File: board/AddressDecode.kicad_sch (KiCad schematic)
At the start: 17 parts, among them U10 74LS154, U11 74F00, U12 74F02, U13 74F08, U14 74F32, U15 74F30, U16 74LS260, U17 74LS154, U18 74F04

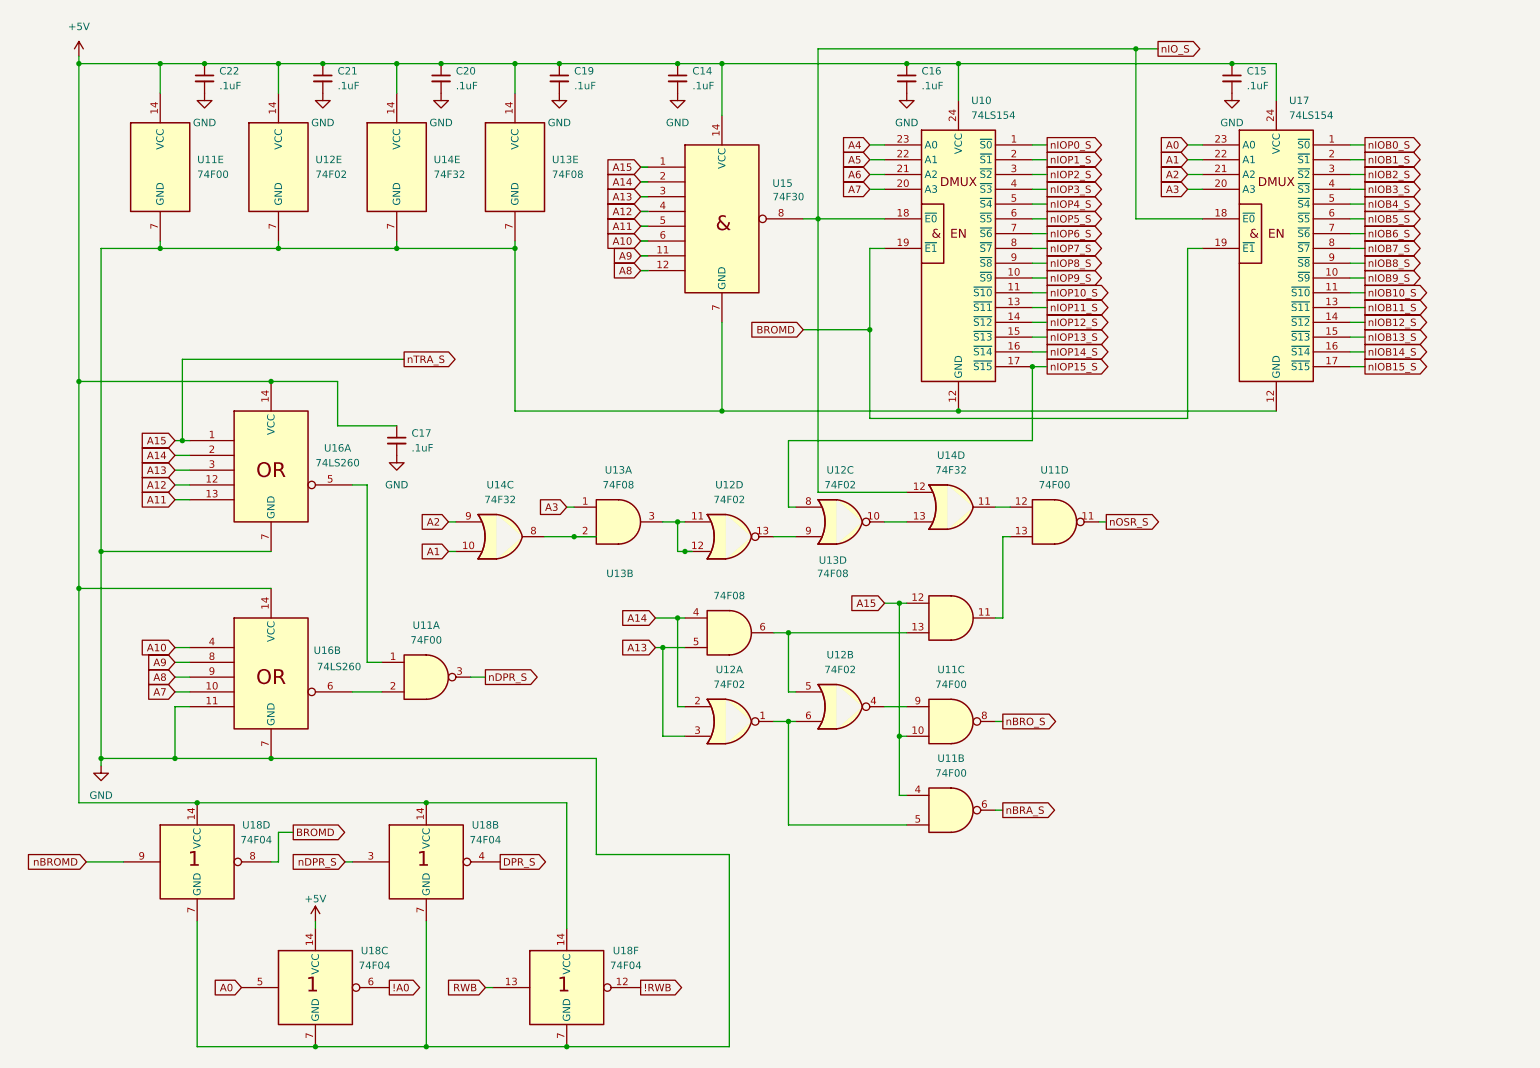
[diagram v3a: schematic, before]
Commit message: More main PCB updates.  Rearranged some things.  Bypass caps near PS connector.  Moved front panel connector to opposite side of board.
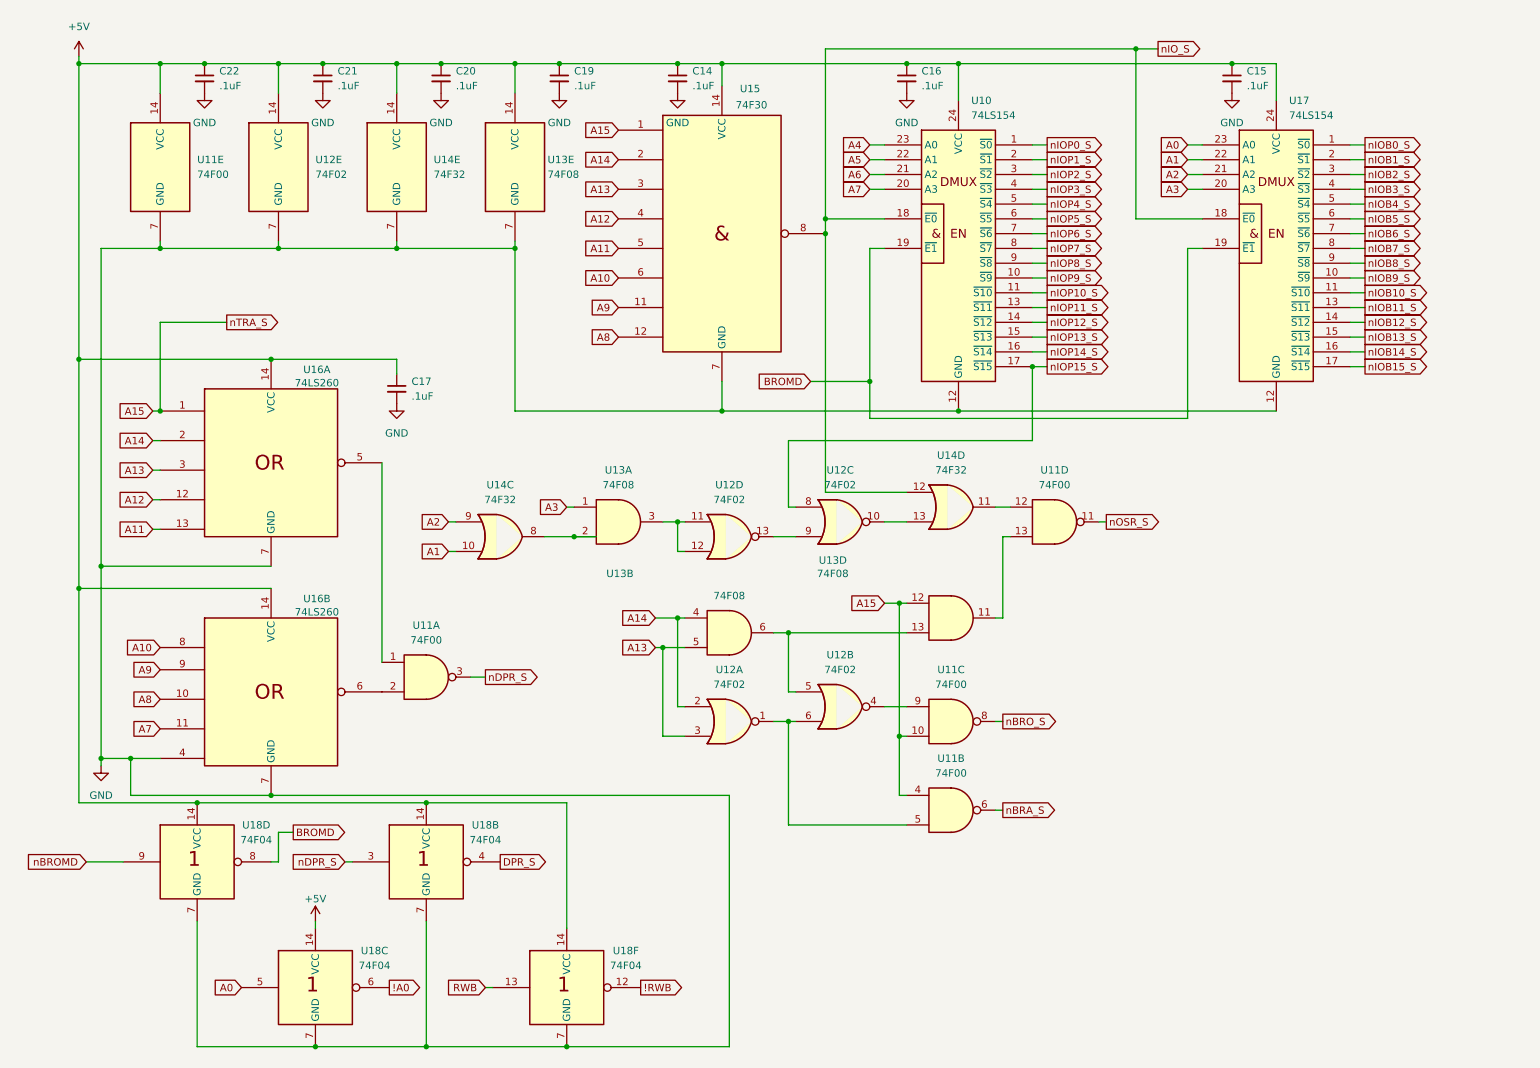
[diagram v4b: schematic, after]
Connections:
- net A10: now also U16.8; no longer U16.4
- net A7: now also U16.11; no longer U16.10
- net A8: now also U16.10; no longer U16.9
- net A9: now also U16.9; no longer U16.8
- net GND: now also U16.4; no longer U16.11
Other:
- moved on the sheet: C17, U15, U16A, U16B

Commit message: Latest main PCB update with FFF1 and FFF2 added and decode logic updated to exclude FFFE and FFFF in nOSROM_S signal
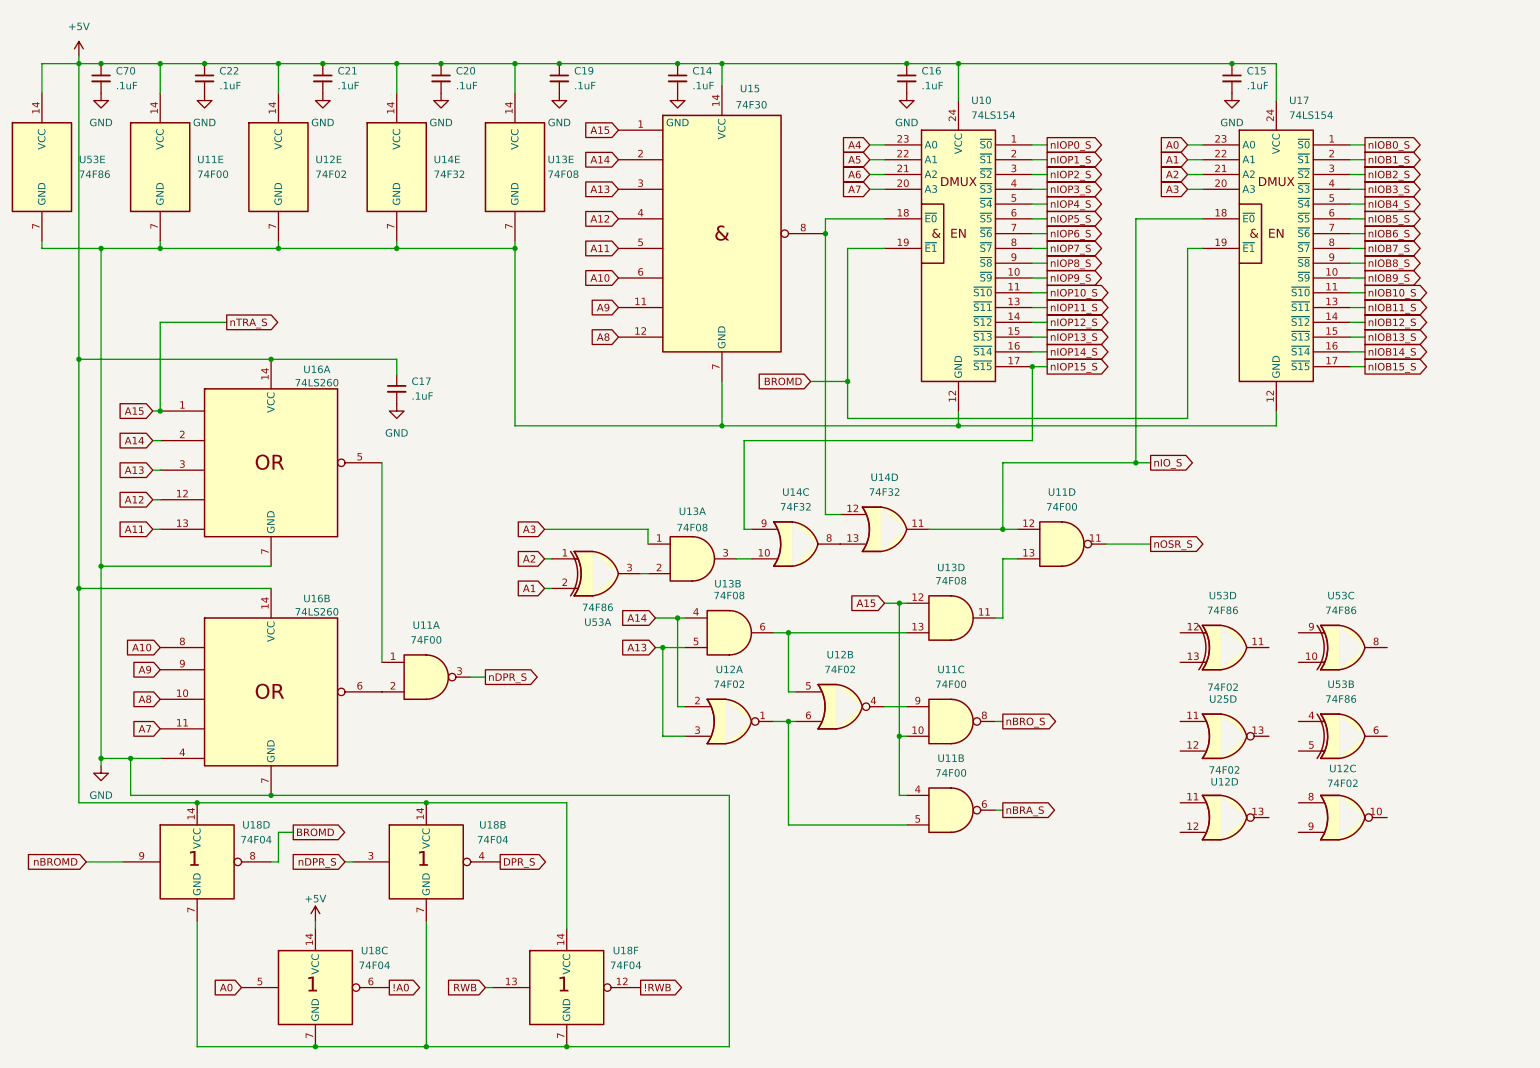
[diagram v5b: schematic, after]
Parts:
- added C70: .1uF, Capacitor_THT:C_Disc_D5.0mm_W2.5mm_P5.00mm, symbol Device:C_Small
- added U25: 74F02, Package_DIP:DIP-14_W7.62mm_Socket_LongPads, symbol 74xx:7402
- added U53: 74F86, Package_DIP:DIP-14_W7.62mm_Socket_LongPads, symbol 74xx:74LS86
- U10, U17: footprint Package_DIP:DIP-24_W15.24mm_LongPads -> Package_DIP:DIP-24_W15.24mm_Socket_LongPads
- U11, U13, U14, U15, U16, U18: footprint Package_DIP:DIP-14_W7.62mm_LongPads -> Package_DIP:DIP-14_W7.62mm_Socket_LongPads
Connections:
- net +5V: now also C70.1, U53.14 (VCC)
- net A1: now also U53.2; no longer U14.10
- net A2: now also U53.1; no longer U14.9
- net GND: now also C70.2, U53.7 (GND)
- net nIOP15_S: now also U14.9; no longer U12.8
- net nIO_S: now also U11.12, U14.11; no longer U10.18 (~{E0}), U14.12, U15.8
- net at U12.13: no longer U12.9
- net at U14.13: now also U14.8; no longer U12.10
- net at U13.2: now also U53.3; no longer U14.8
- new net: U13.3, U14.10
- new net: U10.18 (~{E0}), U14.12, U15.8
- now unconnected: U12.11, U12.12
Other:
- moved on the sheet: U11D, U14D

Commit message: Updated schematics with larger mounting holes (4mm vs 3.2mm) and larger electrolytic cap footprints
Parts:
- U12: footprint Package_DIP:DIP-14_W7.62mm_LongPads -> Package_DIP:DIP-14_W7.62mm_Socket_LongPads
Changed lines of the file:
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@@
 			)
 		)
-		(property "Footprint" "Package_DIP:DIP-14_W7.62mm_LongPads"
+		(property "Footprint" "Package_DIP:DIP-14_W7.62mm_Socket_LongPads"
 			(at 162.56 135.89 0)
 			(effects
@@
 			)
 		)
-		(property "Footprint" "Package_DIP:DIP-14_W7.62mm_LongPads"
+		(property "Footprint" "Package_DIP:DIP-14_W7.62mm_Socket_LongPads"
 			(at 143.51 138.43 0)
 			(effects
@@
 			)
 		)
-		(property "Footprint" "Package_DIP:DIP-14_W7.62mm_LongPads"
+		(property "Footprint" "Package_DIP:DIP-14_W7.62mm_Socket_LongPads"
 			(at 66.04 43.18 0)
 			(effects
@@
 			)
 		)
-		(property "Footprint" "Package_DIP:DIP-14_W7.62mm_LongPads"
+		(property "Footprint" "Package_DIP:DIP-14_W7.62mm_Socket_LongPads"
 			(at 228.6 154.94 0)
 			(effects
@@
 			)
 		)
-		(property "Footprint" "Package_DIP:DIP-14_W7.62mm_LongPads"
+		(property "Footprint" "Package_DIP:DIP-14_W7.62mm_Socket_LongPads"
 			(at 248.92 154.94 0)
 			(effects

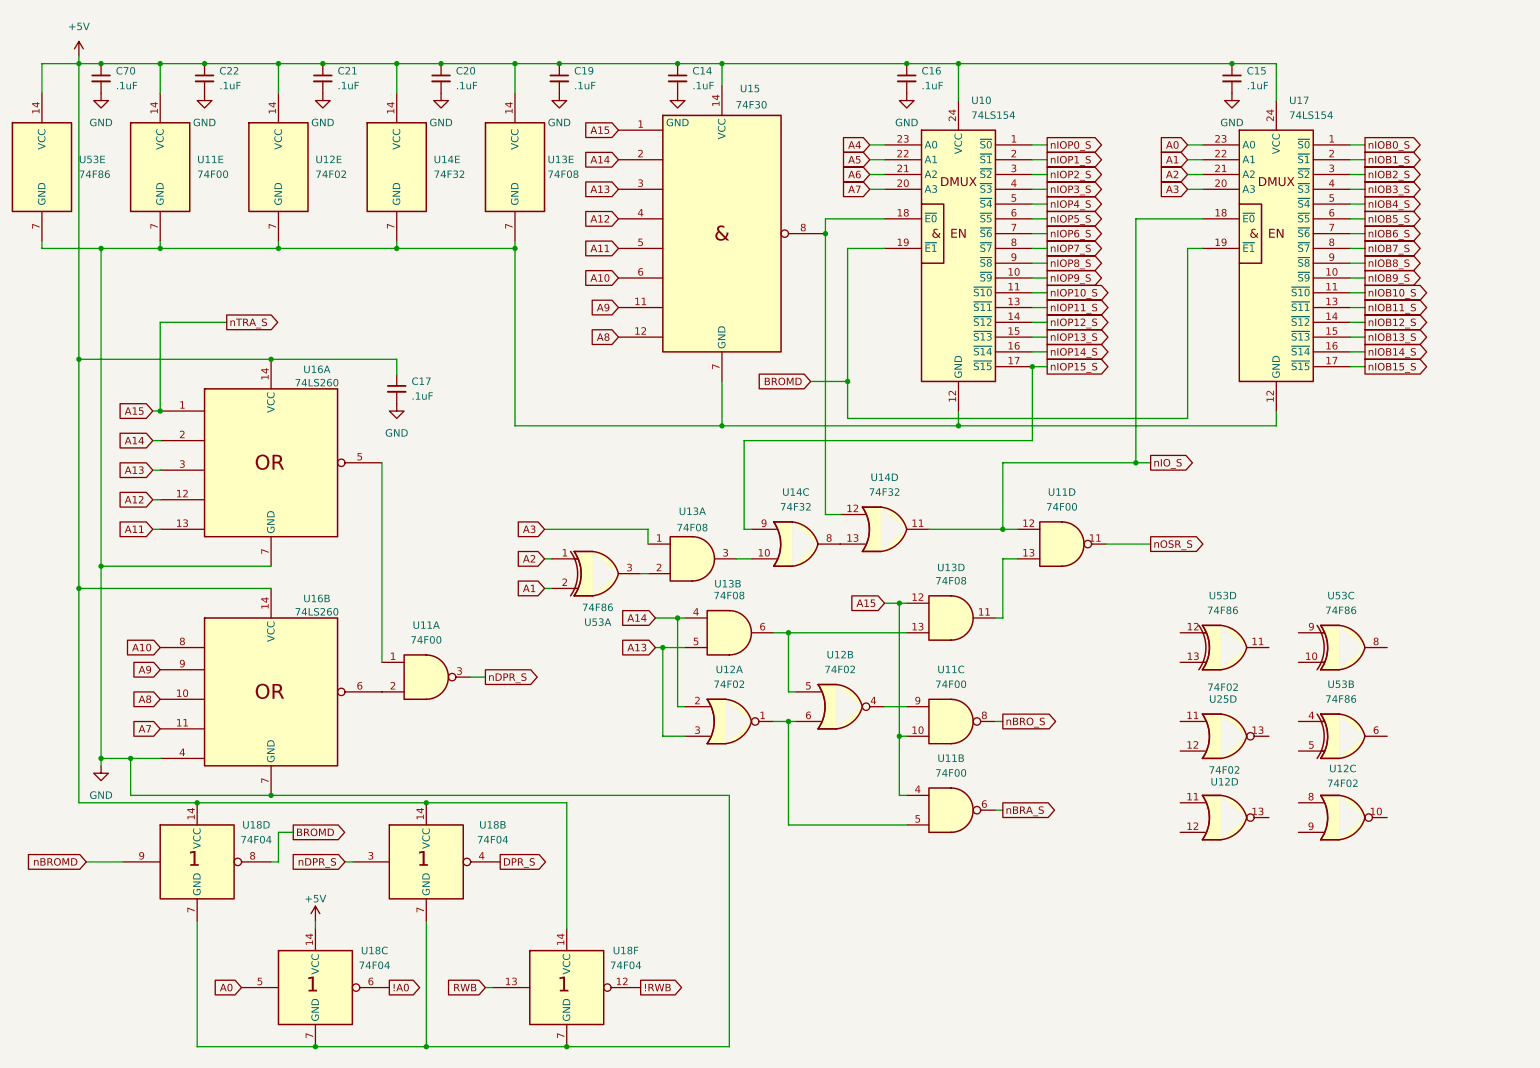
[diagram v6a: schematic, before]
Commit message: Schematic Bus updates, silkscreen updates, position tweaks, and other corrections.
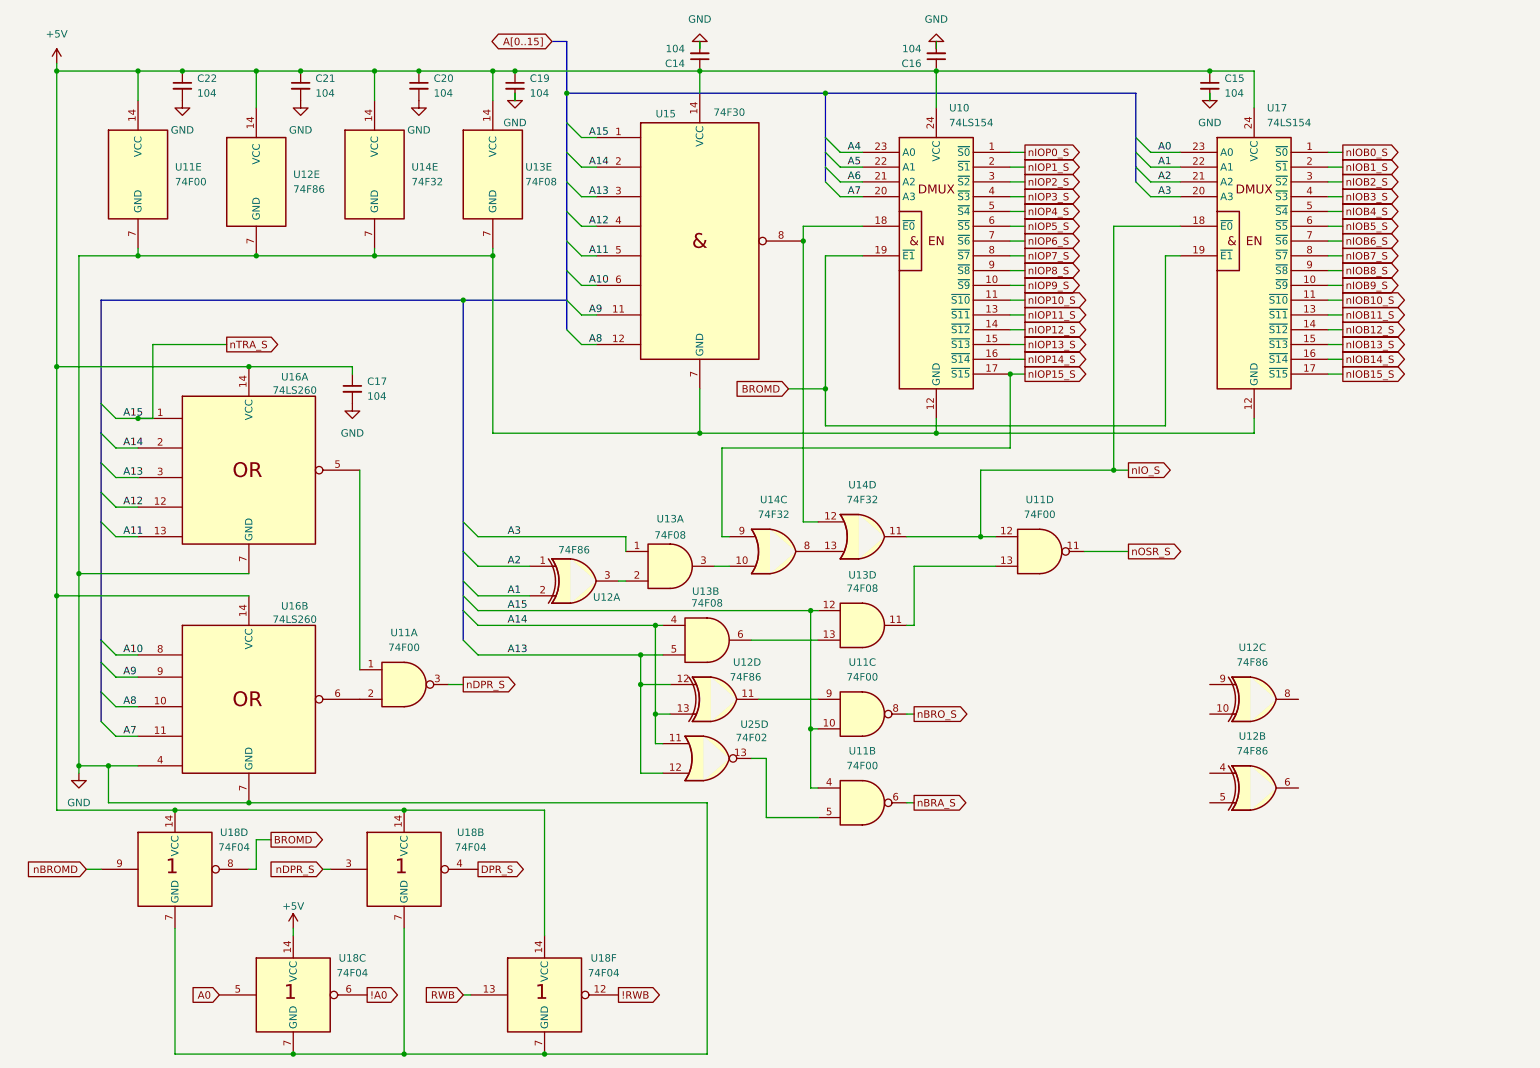
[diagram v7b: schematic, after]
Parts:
- removed C70: .1uF, Capacitor_THT:C_Disc_D5.0mm_W2.5mm_P5.00mm, symbol Device:C_Small
- removed unit 2 of U12
- removed unit 5 of U12
- removed unit 4 of U12
- removed unit 3 of U12
- removed U25: 74F02, Package_DIP:DIP-14_W7.62mm_Socket_LongPads, symbol 74xx:7402
- C14, C15, C16, C17, C19, C20, C21, C22: value .1uF -> 104
- renumbered U53 to U12, U12 to U25
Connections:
- net A13: now also U12.12, U25.12; no longer U25.3
- net A14: now also U12.13, U25.11; no longer U25.2
- net at U11.9: now also U12.11
- net at U11.5: now also U25.13; no longer U25.1
- net A15 renamed nTRA_S
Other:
- company: (none) -> Data Tuning
- title: (none) -> Address Decode Logic
- moved on the sheet: C14, C15, C16, C17, C19, C20, C21, C22, U10, U11A, U11B, U11C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

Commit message: Fixing nBROMD routing, removing unnecessary 7404, and minor other cleanup.
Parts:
- removed unit 4 of U18
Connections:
- net BROMD is gone; now on net +5V: U10.19 (~{E1}), U17.19 (~{E1})
